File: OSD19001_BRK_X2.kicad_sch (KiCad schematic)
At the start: 0 parts

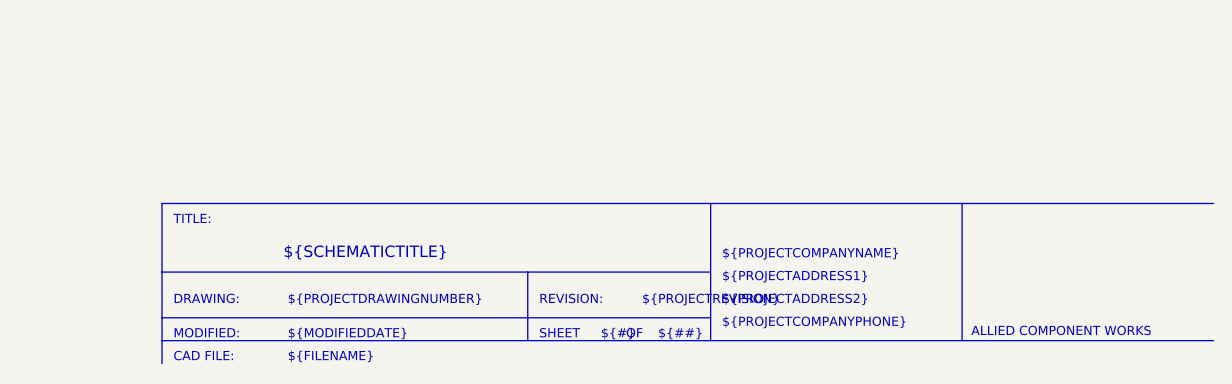
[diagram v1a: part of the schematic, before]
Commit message: Corrected title bar text to match online PDF schematic
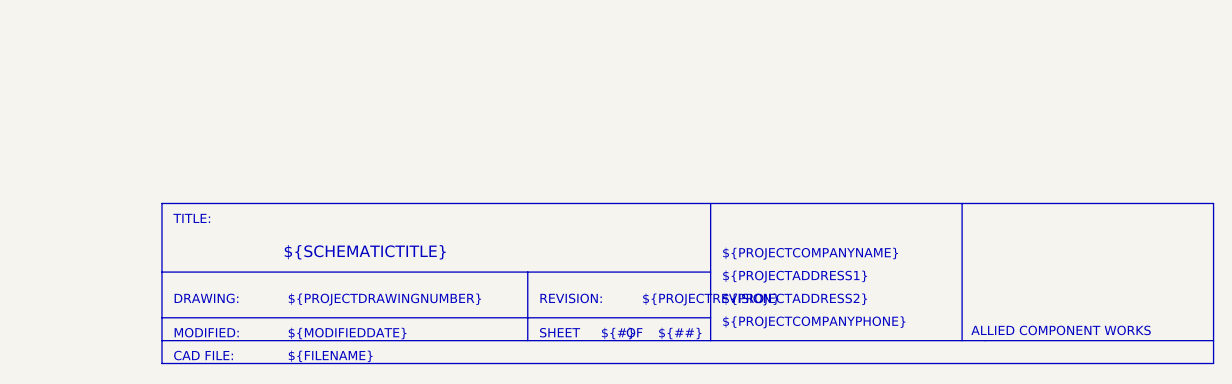
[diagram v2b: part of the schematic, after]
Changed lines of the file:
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@@
+    (stroke (width 0) (type solid) (color 0 0 0 0))
+  )
+  (polyline (pts (xy 375.92 256.54) (xy 375.92 274.32))
+    (stroke (width 0) (type solid) (color 0 0 0 0))
+  )
+  (polyline (pts (xy 375.92 274.32) (xy 259.08 274.32))
     (stroke (width 0) (type solid) (color 0 0 0 0))
   )
